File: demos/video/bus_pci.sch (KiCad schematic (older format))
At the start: 33 parts, among them U1 24C16, U11 S5933_PQ160

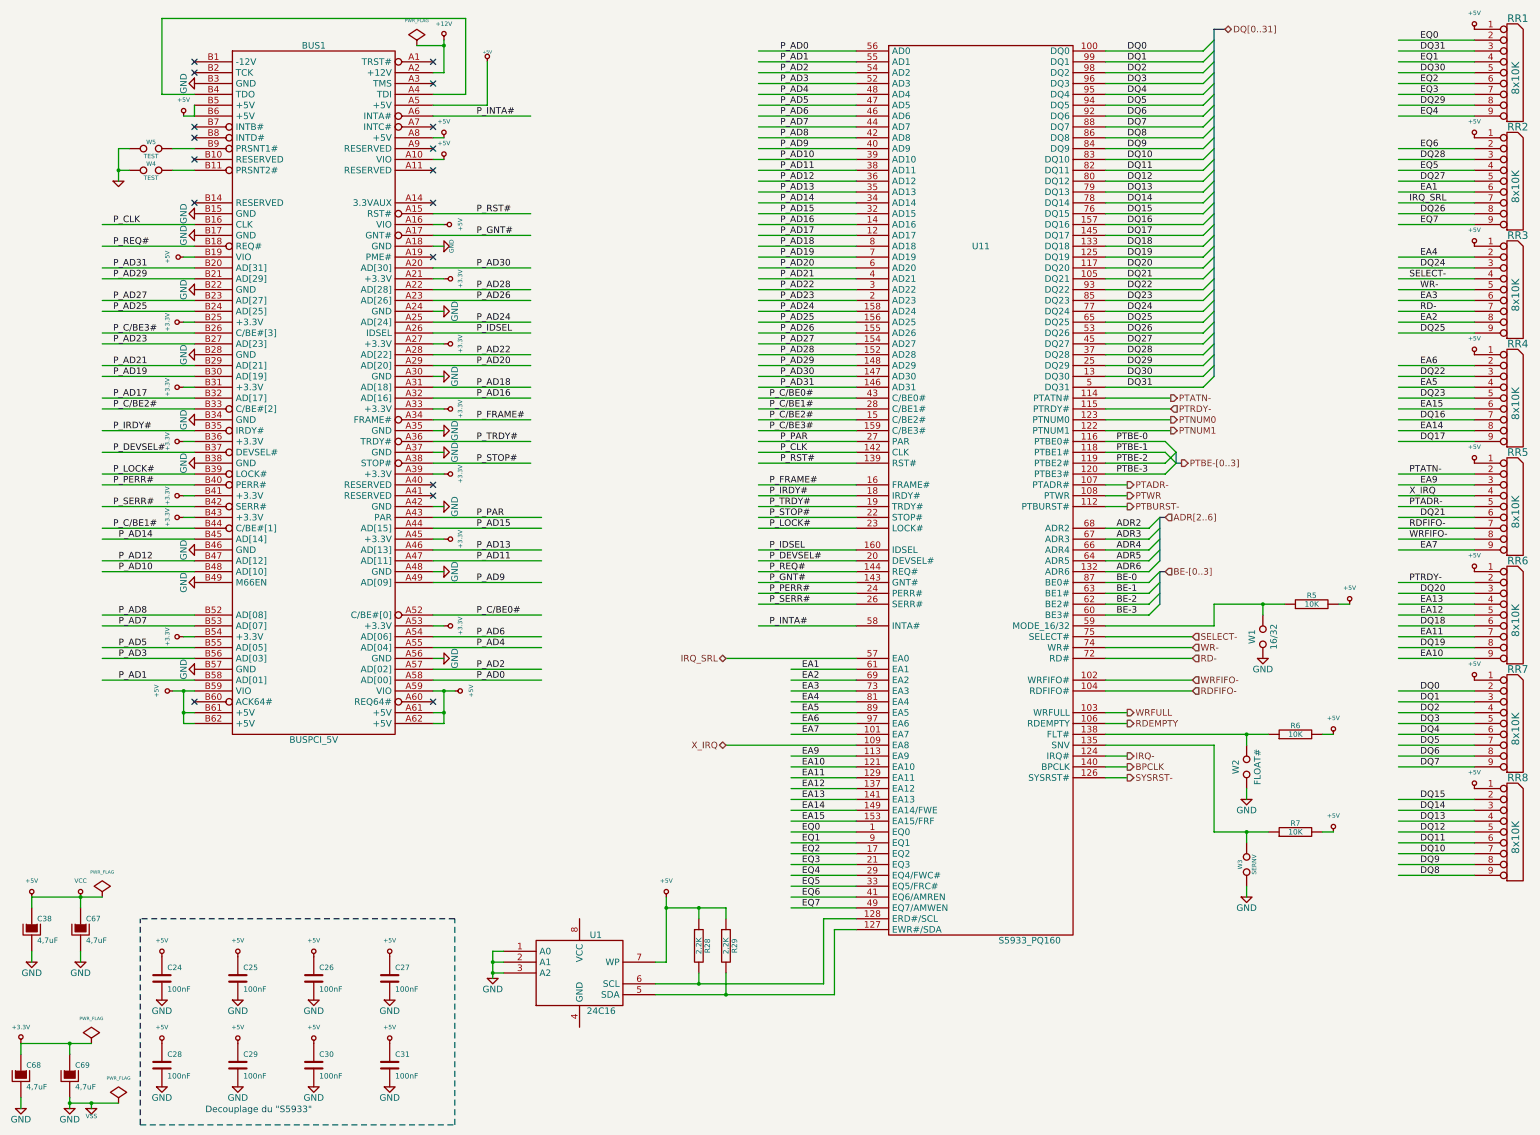
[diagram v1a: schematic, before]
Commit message: Pcbnew: Minor fix in hotkeys. Demos: add an example to use  a local fp-lib-table and local libs, and update schematics and boards.
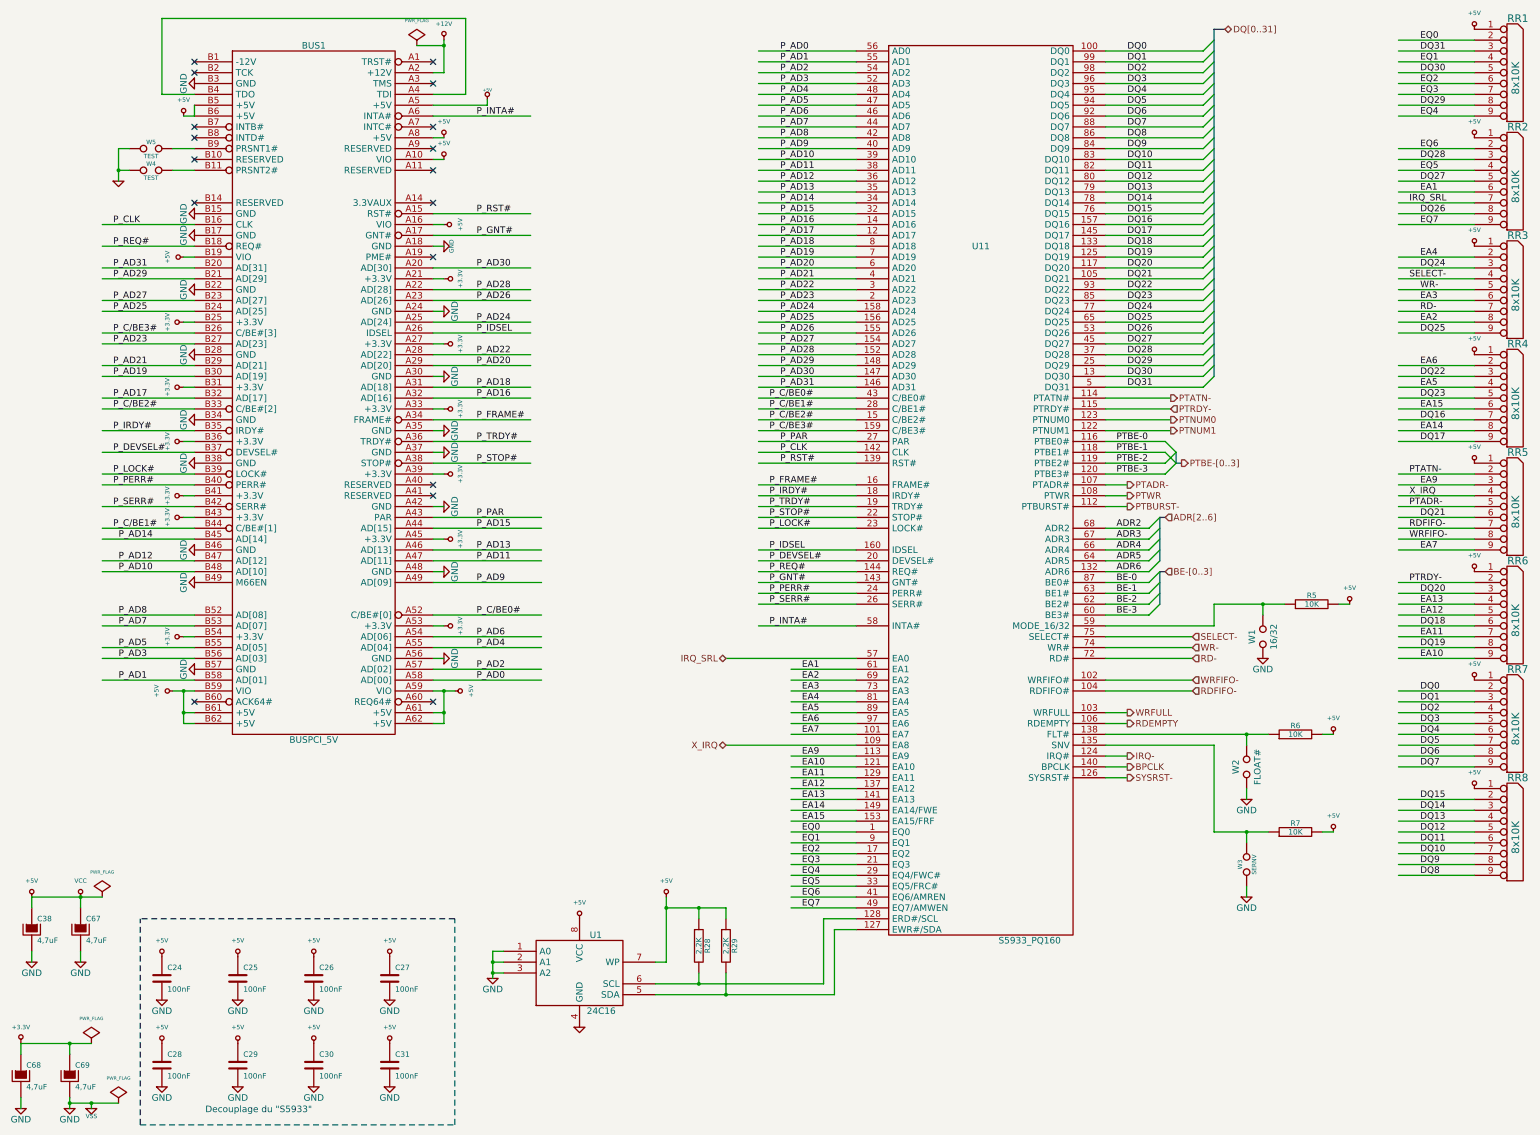
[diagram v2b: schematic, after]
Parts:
- BUS1: footprint (none) -> connect:BUSPCI
- C24, C25, C26, C27, C28, C29, C30, C31, C67, C68, C69, R28, R29, R5, R6, R7: footprint (none) -> lib_smd:SM1206
- C38: footprint (none) -> lib_smd:SM1812L
- RR1, RR2, RR3, RR6, RR8: footprint (none) -> connect:SIL-9
- RR4, RR5, RR7: footprint (none) -> discret:r_pack8
- U1: footprint (none) -> dip_sockets:DIP-8__300
- U11: footprint (none) -> lib_smd:PQFP160
- W1, W2, W3: footprint (none) -> connect:GS2
- W4, W5: footprint (none) -> pin_array:PIN_ARRAY_2X1

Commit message: demos/ schematic tidying
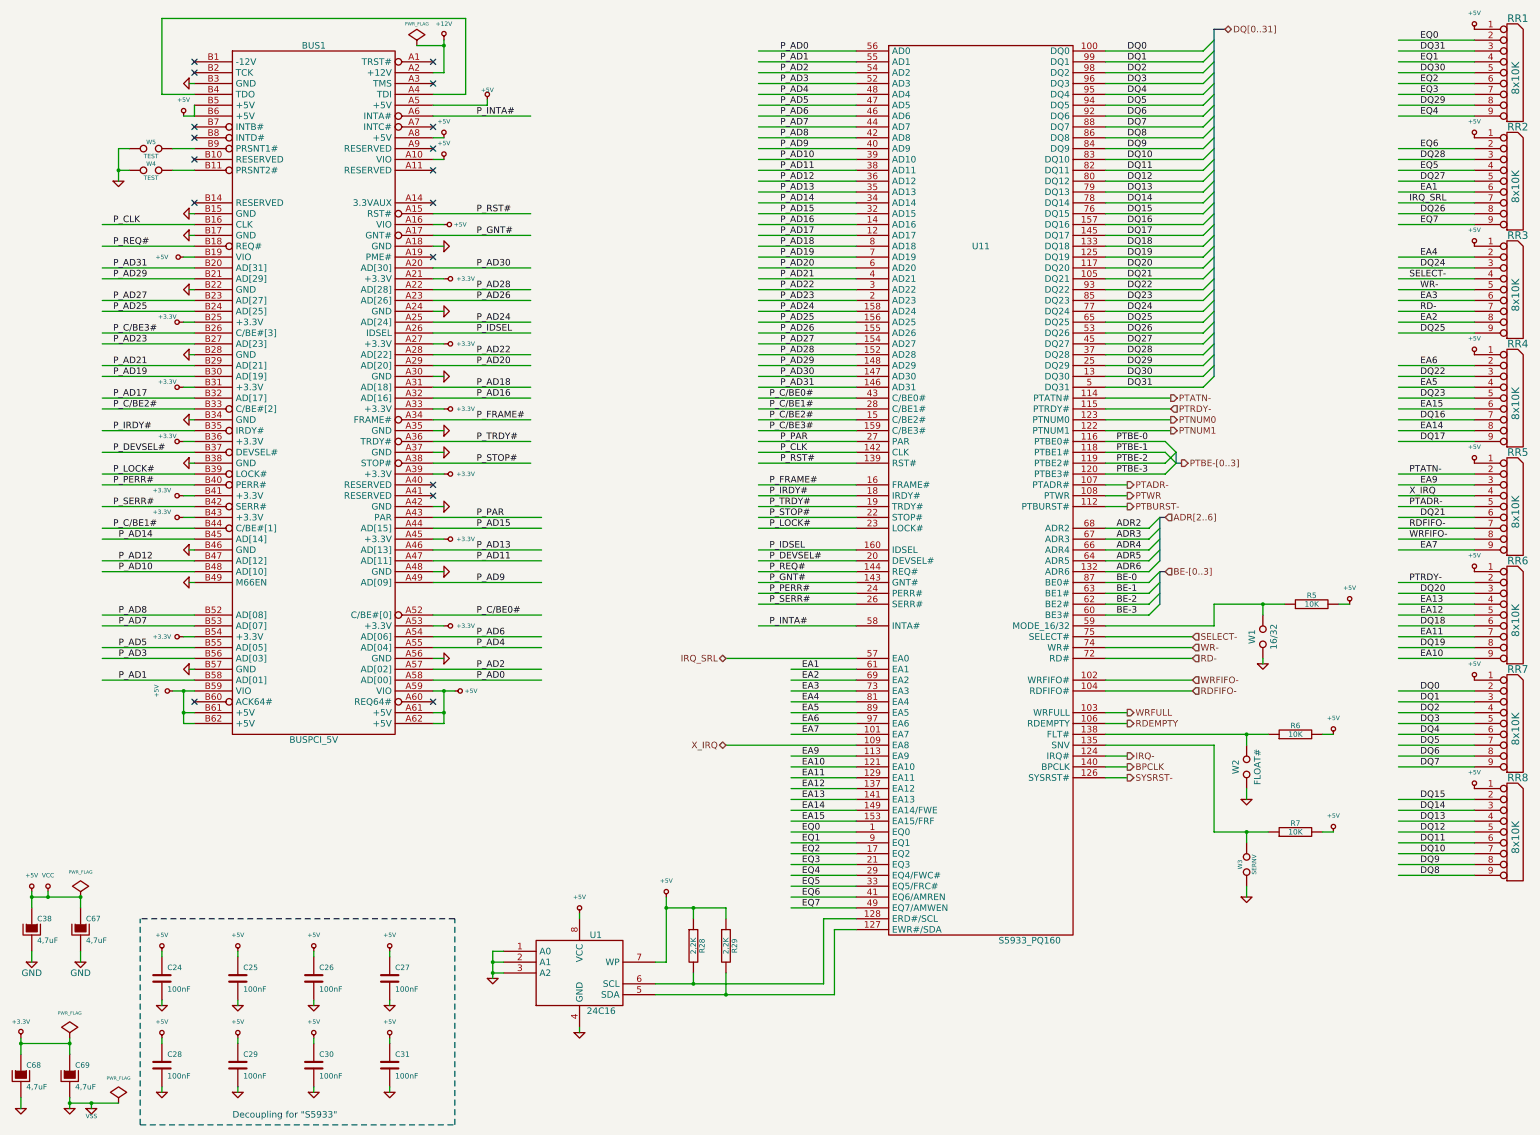
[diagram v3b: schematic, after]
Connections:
- wire segments 345 -> 375
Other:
- note added: "Decoupling for "S5933""
- note removed: "Decouplage du "S5933""
- moved on the sheet: R28

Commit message: polygons in footprint body: fix incorrect calculation of polygons with clearance or outline thickness (fix bug #1511366) Clean demos
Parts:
- BUS1: footprint connect:BUSPCI -> Connect:BUSPCI
- RR1, RR2, RR3, RR6, RR8: footprint connect:SIL-9 -> Connect:SIL-9
- RR4, RR5, RR7: footprint discret:r_pack8 -> Discret:r_pack8
- W1, W2, W3: footprint connect:GS2 -> Connect:GS2
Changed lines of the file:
@@
 EESchema Schematic File Version 2
+LIBS:video_schlib
 LIBS:power
-LIBS:device
-LIBS:transistors
-LIBS:conn
-LIBS:linear
-LIBS:regul
-LIBS:74xx
-LIBS:cmos4000
-LIBS:adc-dac
-LIBS:memory
-LIBS:xilinx
-LIBS:special
-LIBS:analog_switches
-LIBS:motorola
-LIBS:intel
-LIBS:audio
-LIBS:interface
-LIBS:philips
-LIBS:cypress
-LIBS:siliconi
 LIBS:video-cache
 EELAYER 25 0
@@
 F 0 "BUS1" H 3300 7400 60  0000 C CNN
 F 1 "BUSPCI_5V" H 3300 1000 60  0000 C CNN
-F 2 "connect:BUSPCI" H 3300 4200 60  0001 C CNN
+F 2 "Connect:BUSPCI" H 3300 4200 60  0001 C CNN
 F 3 "" H 3300 4200 60  0001 C CNN
 	1    3300 4200
@@
 F 0 "RR1" H 14400 1850 70  0000 C CNN
 F 1 "8x10K" V 14380 1300 70  0000 C CNN
-F 2 "connect:SIL-9" H 14350 1300 60  0001 C CNN
+F 2 "Connect:SIL-9" H 14350 1300 60  0001 C CNN
 F 3 "" H 14350 1300 60  0001 C CNN
 	1    14350 1300
@@
 F 0 "RR2" H 14400 2850 70  0000 C CNN
 F 1 "8x10K" V 14380 2300 70  0000 C CNN
-F 2 "connect:SIL-9" H 14350 2300 60  0001 C CNN
+F 2 "Connect:SIL-9" H 14350 2300 60  0001 C CNN
 F 3 "" H 14350 2300 60  0001 C CNN
 	1    14350 2300
@@
 F 0 "RR3" H 14400 3850 70  0000 C CNN
 F 1 "8x10K" V 14380 3300 70  0000 C CNN
-F 2 "connect:SIL-9" H 14350 3300 60  0001 C CNN
+F 2 "Connect:SIL-9" H 14350 3300 60  0001 C CNN
 F 3 "" H 14350 3300 60  0001 C CNN
 	1    14350 3300
@@
 F 0 "RR4" H 14400 4850 70  0000 C CNN
 F 1 "8x10K" V 14380 4300 70  0000 C CNN
-F 2 "discret:r_pack8" H 14350 4300 60  0001 C CNN
+F 2 "Discret:r_pack8" H 14350 4300 60  0001 C CNN
 F 3 "" H 14350 4300 60  0001 C CNN
 	1    14350 4300
@@
 F 0 "RR5" H 14400 5850 70  0000 C CNN
 F 1 "8x10K" V 14380 5300 70  0000 C CNN
-F 2 "discret:r_pack8" H 14350 5300 60  0001 C CNN
+F 2 "Discret:r_pack8" H 14350 5300 60  0001 C CNN
 F 3 "" H 14350 5300 60  0001 C CNN
 	1    14350 5300
@@
 F 0 "RR6" H 14400 6850 70  0000 C CNN
 F 1 "8x10K" V 14380 6300 70  0000 C CNN
-F 2 "connect:SIL-9" H 14350 6300 60  0001 C CNN
+F 2 "Connect:SIL-9" H 14350 6300 60  0001 C CNN
 F 3 "" H 14350 6300 60  0001 C CNN
 	1    14350 6300
@@
 F 0 "RR7" H 14400 7850 70  0000 C CNN
 F 1 "8x10K" V 14380 7300 70  0000 C CNN
-F 2 "discret:r_pack8" H 14350 7300 60  0001 C CNN
+F 2 "Discret:r_pack8" H 14350 7300 60  0001 C CNN
 F 3 "" H 14350 7300 60  0001 C CNN
 	1    14350 7300
@@
 F 0 "RR8" H 14400 8850 70  0000 C CNN
 F 1 "8x10K" V 14380 8300 70  0000 C CNN
-F 2 "connect:SIL-9" H 14350 8300 60  0001 C CNN
+F 2 "Connect:SIL-9" H 14350 8300 60  0001 C CNN
 F 3 "" H 14350 8300 60  0001 C CNN
 	1    14350 8300
@@
 F 0 "W2" H 11900 7750 60  0000 C CNN
 F 1 "FLOAT#" H 11900 7550 60  0000 C CNN
-F 2 "connect:GS2" H 11900 7650 60  0001 C CNN
+F 2 "Connect:GS2" H 11900 7650 60  0001 C CNN
 F 3 "" H 11900 7650 60  0001 C CNN
 	1    11900 7650
@@
 F 0 "W3" H 11900 8610 40  0000 C CNN
 F 1 "SERNV" H 11900 8480 40  0000 C CNN
-F 2 "connect:GS2" H 11900 8550 60  0001 C CNN
+F 2 "Connect:GS2" H 11900 8550 60  0001 C CNN
 F 3 "" H 11900 8550 60  0001 C CNN
 	1    11900 8550
@@
 F 0 "W1" H 12050 6550 60  0000 C CNN
 F 1 "16/32" H 12050 6350 60  0000 C CNN
-F 2 "connect:GS2" H 12050 6450 60  0001 C CNN
+F 2 "Connect:GS2" H 12050 6450 60  0001 C CNN
 F 3 "" H 12050 6450 60  0001 C CNN
 	1    12050 6450

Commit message: merge from production git:e53c3af 21.04.2017
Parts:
- BUS1: footprint Connect:BUSPCI -> Connectors:BUSPCI
- RR1, RR2, RR3, RR6, RR8: footprint Connect:SIL-9 -> Connectors:SIL-9
- W1, W2, W3: footprint Connect:GS2 -> Connectors:GS2
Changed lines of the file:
@@
 LIBS:power
 LIBS:video-cache
-EELAYER 25 0
+EELAYER 26 0
 EELAYER END
 $Descr A3 16535 11693
@@
 F 0 "BUS1" H 3300 7400 60  0000 C CNN
 F 1 "BUSPCI_5V" H 3300 1000 60  0000 C CNN
-F 2 "Connect:BUSPCI" H 3300 4200 60  0001 C CNN
+F 2 "Connectors:BUSPCI" H 3300 4200 60  0001 C CNN
 F 3 "" H 3300 4200 60  0001 C CNN
 	1    3300 4200
@@
 F 0 "RR1" H 14400 1850 70  0000 C CNN
 F 1 "8x10K" V 14380 1300 70  0000 C CNN
-F 2 "Connect:SIL-9" H 14350 1300 60  0001 C CNN
+F 2 "Connectors:SIL-9" H 14350 1300 60  0001 C CNN
 F 3 "" H 14350 1300 60  0001 C CNN
 	1    14350 1300
@@
 F 0 "RR2" H 14400 2850 70  0000 C CNN
 F 1 "8x10K" V 14380 2300 70  0000 C CNN
-F 2 "Connect:SIL-9" H 14350 2300 60  0001 C CNN
+F 2 "Connectors:SIL-9" H 14350 2300 60  0001 C CNN
 F 3 "" H 14350 2300 60  0001 C CNN
 	1    14350 2300
@@
 F 0 "RR3" H 14400 3850 70  0000 C CNN
 F 1 "8x10K" V 14380 3300 70  0000 C CNN
-F 2 "Connect:SIL-9" H 14350 3300 60  0001 C CNN
+F 2 "Connectors:SIL-9" H 14350 3300 60  0001 C CNN
 F 3 "" H 14350 3300 60  0001 C CNN
 	1    14350 3300
@@
 F 0 "RR6" H 14400 6850 70  0000 C CNN
 F 1 "8x10K" V 14380 6300 70  0000 C CNN
-F 2 "Connect:SIL-9" H 14350 6300 60  0001 C CNN
+F 2 "Connectors:SIL-9" H 14350 6300 60  0001 C CNN
 F 3 "" H 14350 6300 60  0001 C CNN
 	1    14350 6300
@@
 F 0 "RR8" H 14400 8850 70  0000 C CNN
 F 1 "8x10K" V 14380 8300 70  0000 C CNN
-F 2 "Connect:SIL-9" H 14350 8300 60  0001 C CNN
+F 2 "Connectors:SIL-9" H 14350 8300 60  0001 C CNN
 F 3 "" H 14350 8300 60  0001 C CNN
 	1    14350 8300
@@
 F 0 "W2" H 11900 7750 60  0000 C CNN
 F 1 "FLOAT#" H 11900 7550 60  0000 C CNN
-F 2 "Connect:GS2" H 11900 7650 60  0001 C CNN
+F 2 "Connectors:GS2" H 11900 7650 60  0001 C CNN
 F 3 "" H 11900 7650 60  0001 C CNN
 	1    11900 7650
@@
 F 0 "W3" H 11900 8610 40  0000 C CNN
 F 1 "SERNV" H 11900 8480 40  0000 C CNN
-F 2 "Connect:GS2" H 11900 8550 60  0001 C CNN
+F 2 "Connectors:GS2" H 11900 8550 60  0001 C CNN
 F 3 "" H 11900 8550 60  0001 C CNN
 	1    11900 8550
@@
 F 0 "W1" H 12050 6550 60  0000 C CNN
 F 1 "16/32" H 12050 6350 60  0000 C CNN
-F 2 "Connect:GS2" H 12050 6450 60  0001 C CNN
+F 2 "Connectors:GS2" H 12050 6450 60  0001 C CNN
 F 3 "" H 12050 6450 60  0001 C CNN
 	1    12050 6450
